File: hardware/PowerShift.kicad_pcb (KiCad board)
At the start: 2 copper layers, 50 x 100 mm, 62 parts, among them J1 Barrel_Jack, J10 SHIFT_IN, J11 JST-ZR, J12 JST-ZR, J14 JST-ZR, J2 MICRO_USB, J3 JST-ZR, J4 JST-ZR, J5 SHIFT_IN, J6 SHIFT_IN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

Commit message: All on board
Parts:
- J10: moved to B.Cu
- J7: footprint kuro:3x2_1.27mm_SMD_header -> Pin_Headers:Pin_Header_Angled_2x03_Pitch2.54mm
- moved R2 134.3 mm to (85.0, 81.0), turned to 0 degrees
- moved R1 133.0 mm to (85.0, 83.0), turned to 0 degrees
- moved J6 123.1 mm to (89.0, 77.0), turned to 0 degrees
- moved C9 116.1 mm to (93.2, 74.0), turned to 90 degrees
- moved U6 113.6 mm to (96.5, 74.0), turned to 0 degrees
- moved J2 112.6 mm to (85.0, 52.0)
- moved C11 110.9 mm to (90.2, 73.0), turned to 180 degrees
- moved C15 110.2 mm to (98.0, 65.5)
- moved C16 110.2 mm to (98.0, 70.0)
- moved Y1 110.2 mm to (95.0, 67.8)
- moved R4 108.9 mm to (95.0, 60.0), turned to 180 degrees
- moved D1 108.9 mm to (95.0, 62.2)
- moved C10 108.3 mm to (83.2, 60.0)
- moved U9 108.3 mm to (87.0, 66.5)
- moved R3 108.1 mm to (80.0, 65.2)
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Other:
- board size 50 x 100 mm -> 50 x 90 mm

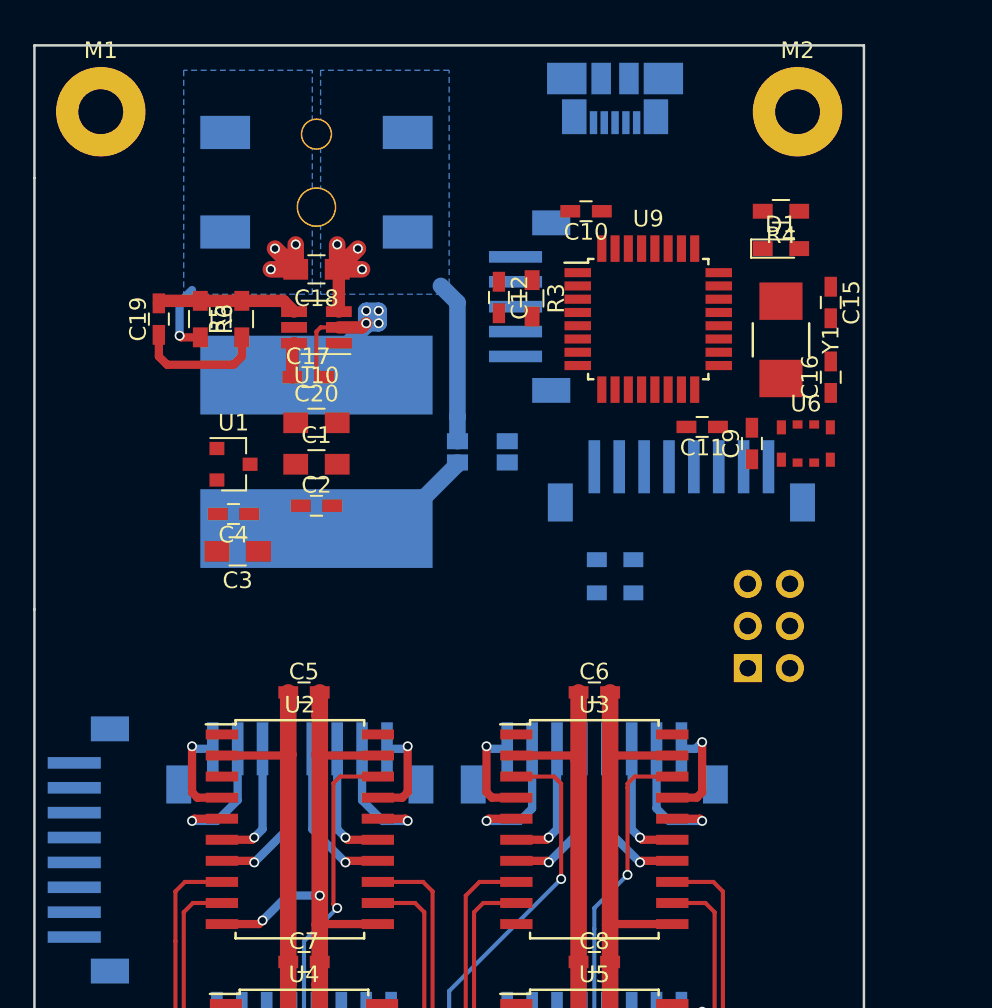
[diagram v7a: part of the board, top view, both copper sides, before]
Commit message: GND plane and 3V3 supply
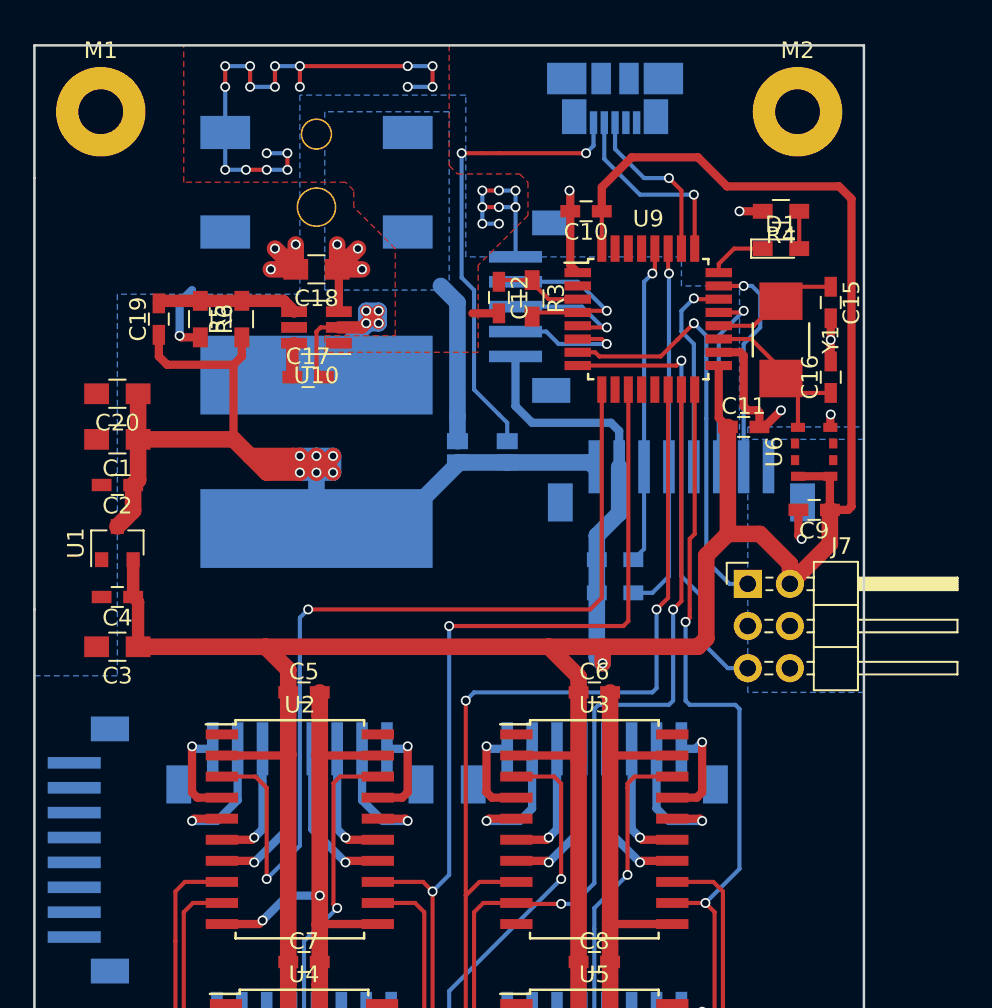
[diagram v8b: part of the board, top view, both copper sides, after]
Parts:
- J7: moved to F.Cu
- moved C20 12.1 mm to (55.0, 71.0), turned to 180 degrees
- moved C1 12.1 mm to (55.0, 73.8), turned to 180 degrees
- moved C2 12.1 mm to (55.0, 76.5), turned to 180 degrees
- moved C3 9.25 mm to (55.0, 86.2)
- moved C4 8.60 mm to (55.0, 83.2)
- moved U1 8.46 mm to (55.0, 80.0), turned to 90 degrees
- moved C9 5.48 mm to (97.0, 78.0), turned to 180 degrees
- moved J7 5.08 mm to (93.0, 82.5)
- moved C11 2.50 mm to (92.8, 73.0), turned to 0 degrees
- moved U6 0.71 mm to (97.0, 74.5), turned to 90 degrees
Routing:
- net +3V3: track 120.4 -> 265.5 mm, vias 0 -> 1
- net GND: track 170.5 -> 234.5 mm, vias 10 -> 42
- net /SER_IN: track 0.00 -> 56.3 mm, vias 0 -> 2
- net VPP: track 18.1 -> 69.1 mm, vias 0 -> 6
- net /~SRCLR: track 84.2 -> 126.1 mm, vias 8 -> 10
- net /SRCK: track 84.9 -> 126.1 mm, vias 8 -> 10
- net /~G: track 79.2 -> 118.9 mm, vias 0 -> 2
- net /RCK: track 79.7 -> 114.7 mm, vias 0 -> 2
- net Net-(J2-Pad1): track 0.00 -> 28.0 mm, vias 0 -> 2
- net /PDI_C: track 0.00 -> 27.3 mm, vias 0 -> 1
- net /PDI_D: track 0.00 -> 25.6 mm, vias 0 -> 1
- net /SCL: track 0.00 -> 22.3 mm, vias 0 -> 1
- net /SDA: track 0.00 -> 19.3 mm, vias 0 -> 1
- net /XCK: track 0.00 -> 13.5 mm, vias 0 -> 1
- net /RX: track 0.00 -> 12.3 mm, vias 0 -> 1
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- added copper zone on F.Cu, net GND
